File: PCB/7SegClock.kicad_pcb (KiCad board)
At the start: 2 copper layers, 19 parts, among them CON1 USB-MINI-B, Q1 NPN, U1 P8X32A, U2 24LC256, U3 FT232RL, U4 DS3231, U6 DS3231, X1 5mhz CRYSTAL

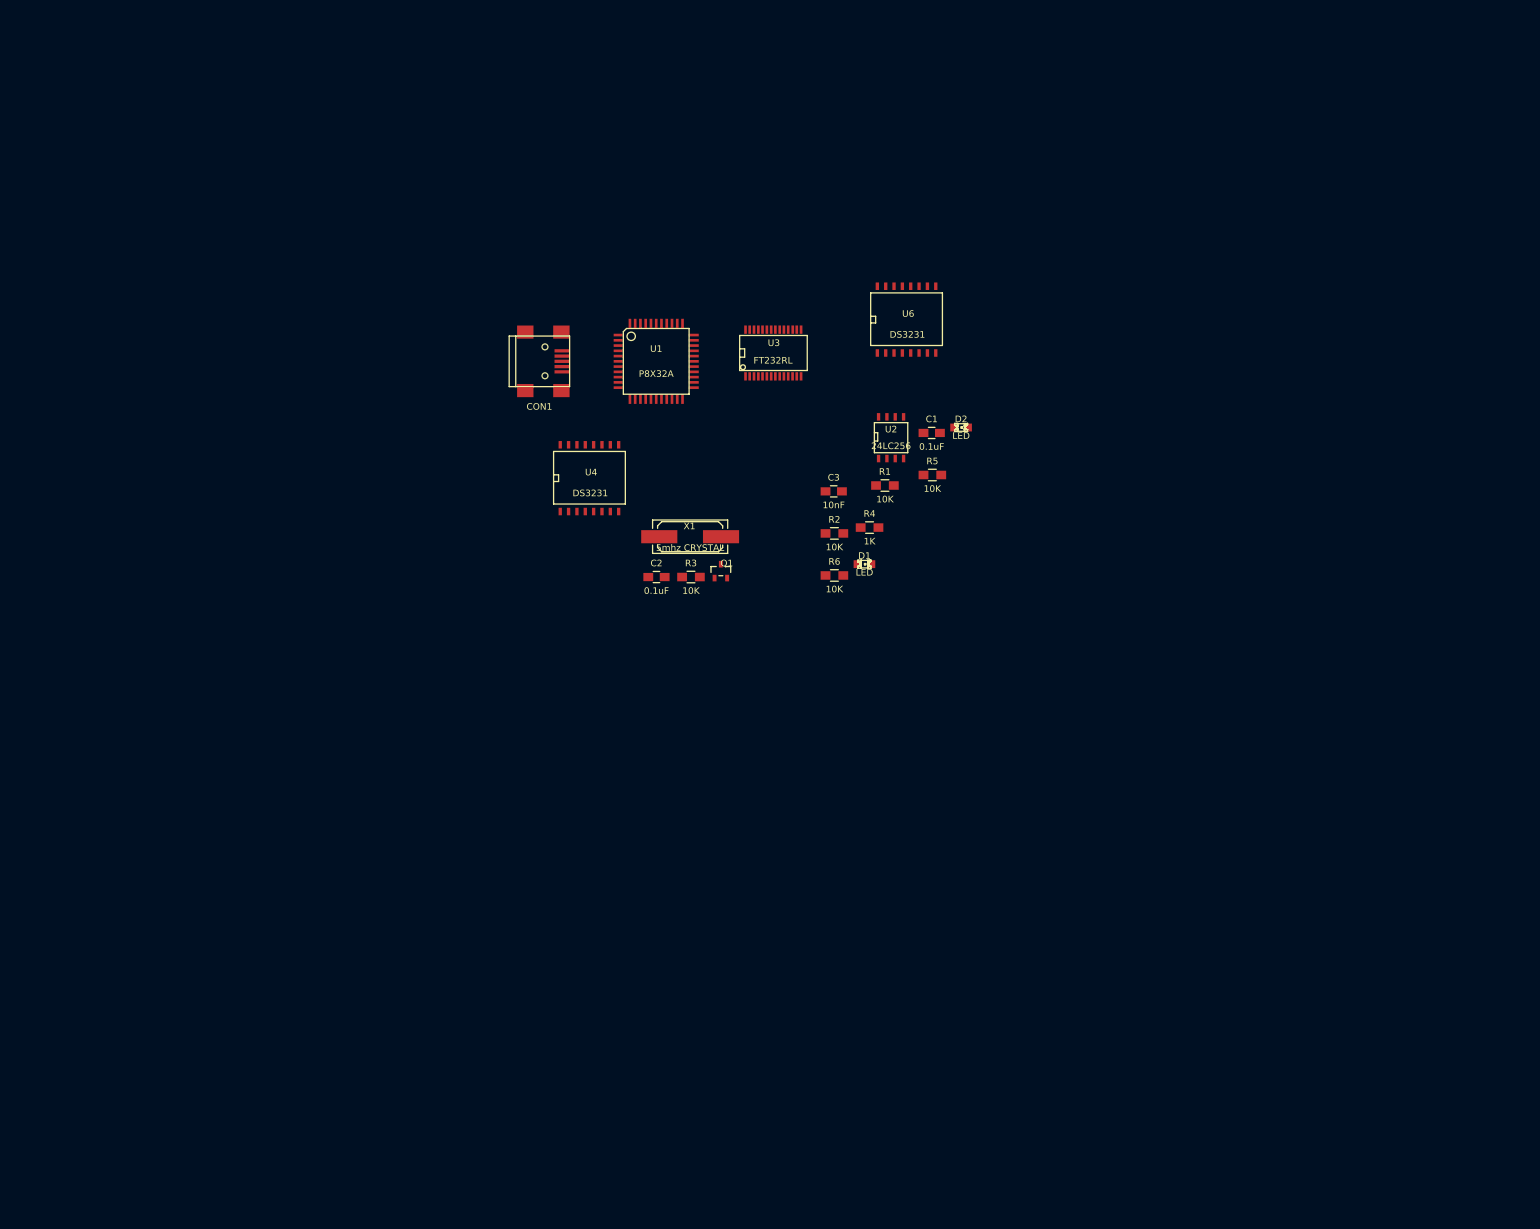
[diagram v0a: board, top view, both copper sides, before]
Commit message: Worked on PCB, added FPGA.
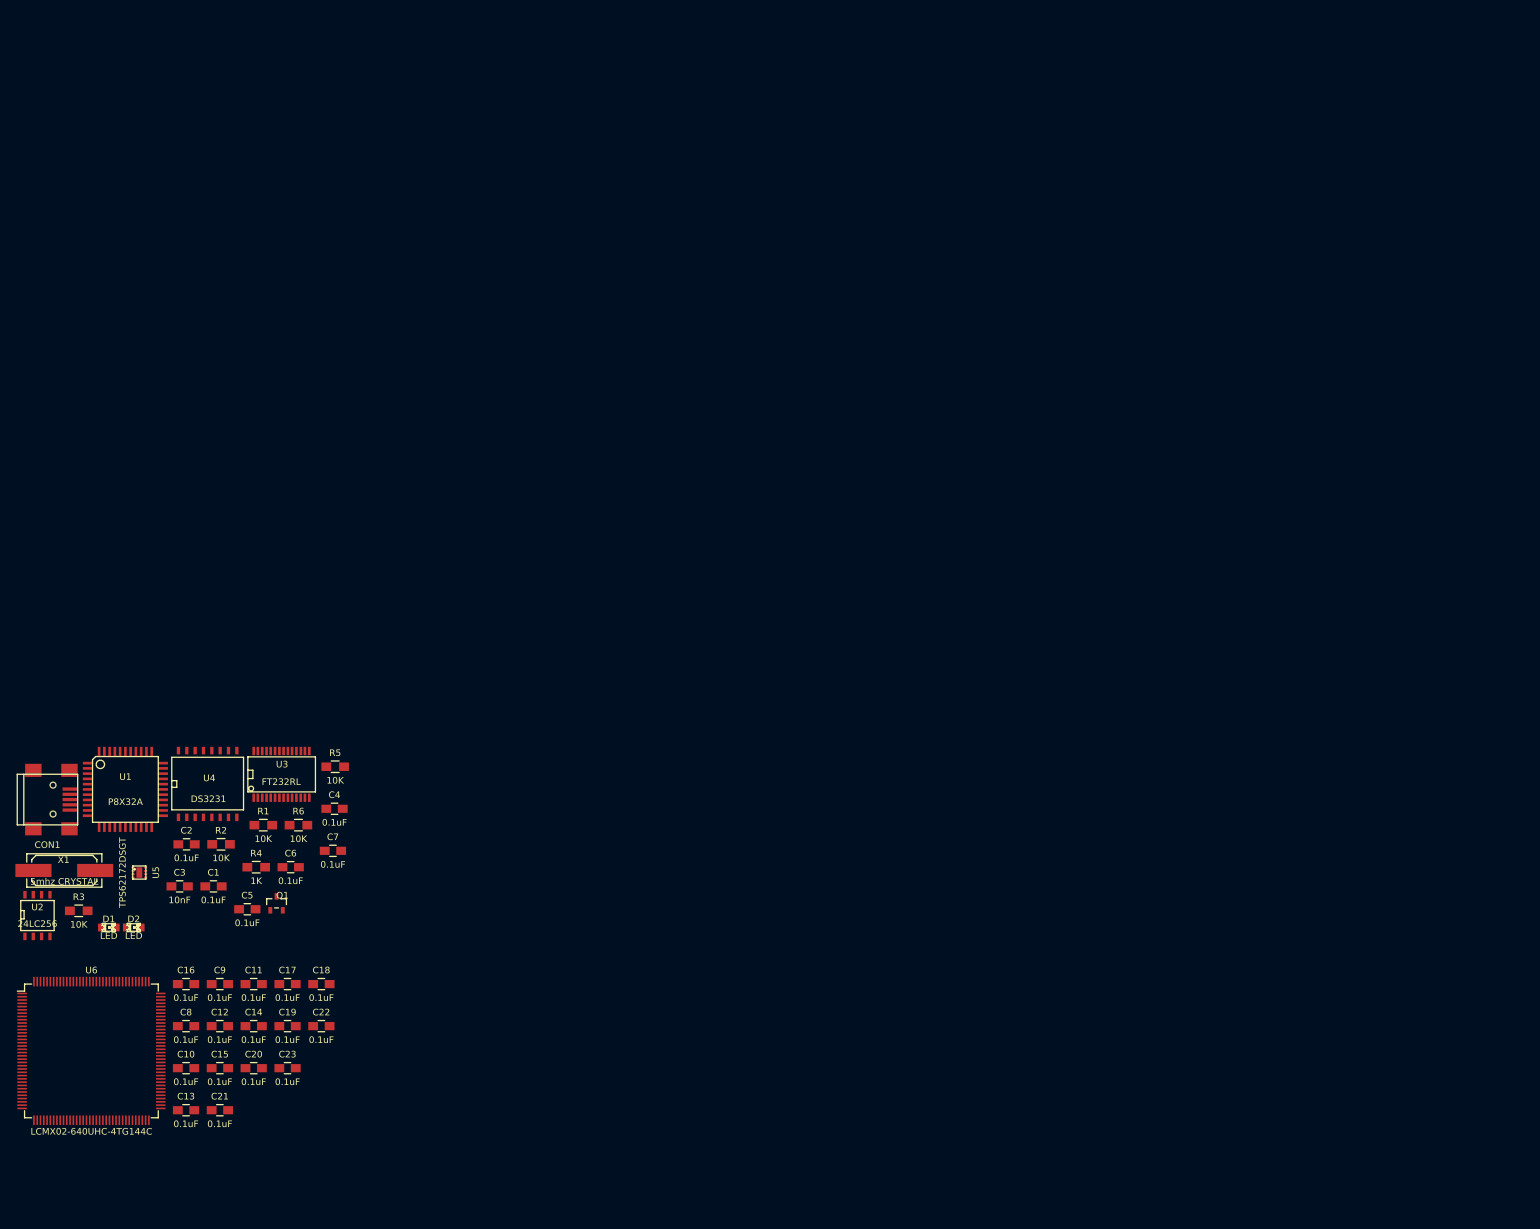
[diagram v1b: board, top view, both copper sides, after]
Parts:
- added C10: 0.1uF, Capacitors_SMD:C_0805_HandSoldering, F.Cu at (49.1, 178.7)
- added C11: 0.1uF, Capacitors_SMD:C_0805_HandSoldering, F.Cu at (59.4, 165.9)
- added C12: 0.1uF, Capacitors_SMD:C_0805_HandSoldering, F.Cu at (54.2, 172.3)
- added C13: 0.1uF, Capacitors_SMD:C_0805_HandSoldering, F.Cu at (49.1, 185.1)
- added C14: 0.1uF, Capacitors_SMD:C_0805_HandSoldering, F.Cu at (59.4, 172.3)
- added C15: 0.1uF, Capacitors_SMD:C_0805_HandSoldering, F.Cu at (54.2, 178.7)
- added C16: 0.1uF, Capacitors_SMD:C_0805_HandSoldering, F.Cu at (49.1, 165.9)
- added C17: 0.1uF, Capacitors_SMD:C_0805_HandSoldering, F.Cu at (64.5, 165.9)
- added C18: 0.1uF, Capacitors_SMD:C_0805_HandSoldering, F.Cu at (69.7, 165.9)
- added C19: 0.1uF, Capacitors_SMD:C_0805_HandSoldering, F.Cu at (64.5, 172.3)
- added C20: 0.1uF, Capacitors_SMD:C_0805_HandSoldering, F.Cu at (59.4, 178.7)
- added C21: 0.1uF, Capacitors_SMD:C_0805_HandSoldering, F.Cu at (54.2, 185.1)
- added C22: 0.1uF, Capacitors_SMD:C_0805_HandSoldering, F.Cu at (69.7, 172.3)
- added C23: 0.1uF, Capacitors_SMD:C_0805_HandSoldering, F.Cu at (64.5, 178.7)
- added C4: 0.1uF, Capacitors_SMD:C_0805_HandSoldering, F.Cu at (71.7, 139.2)
- added C5: 0.1uF, Capacitors_SMD:C_0805_HandSoldering, F.Cu at (58.4, 154.5)
- added C6: 0.1uF, Capacitors_SMD:C_0805_HandSoldering, F.Cu at (65.0, 148.1)
- added C7: 0.1uF, Capacitors_SMD:C_0805_HandSoldering, F.Cu at (71.4, 145.6)
- added C8: 0.1uF, Capacitors_SMD:C_0805_HandSoldering, F.Cu at (49.1, 172.3)
- added C9: 0.1uF, Capacitors_SMD:C_0805_HandSoldering, F.Cu at (54.2, 165.9)
- added U5: TPS62172DSGT, SMD_Packages:WSON-8-1EP, F.Cu at (42.0, 148.9)
- U6: value DS3231 -> LCMX02-640UHC-4TG144C; footprint SMD_Packages:SO-16-W -> Housings_QFP:TQFP-144_20x20mm_Pitch0.5mm
- moved U6 166.7 mm to (34.7, 176.1)
- moved U2 148.9 mm to (26.5, 155.5)
- moved D2 147.1 mm to (41.1, 157.3)
- moved C1 129.3 mm to (53.3, 151.0)
- moved D1 127.6 mm to (37.3, 157.3)
- moved C3 116.3 mm to (48.1, 151.0)
- moved X1 108.0 mm to (30.6, 148.6)
- moved R1 107.8 mm to (60.8, 141.7)
- moved R4 106.7 mm to (59.8, 148.1)
- moved R3 106.1 mm to (32.8, 154.7)
- moved R2 104.7 mm to (54.4, 144.6)
- moved U1 103.8 mm to (39.9, 136.3)
- moved R5 101.2 mm to (71.8, 132.8)
- moved CON1 100.3 mm to (28.0, 137.8)
- moved U3 98.6 mm to (63.6, 134.0)
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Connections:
- net /Lattice MACHXO2/RST renamed Net-(U6-Pad4)
- net Net-(U1-Pad20) renamed /Lattice MACHXO2/CS_PWM
- net Net-(U1-Pad21) renamed /Lattice MACHXO2/CS_Clock
- net Net-(U1-Pad22) renamed /Lattice MACHXO2/CLK
- net Net-(U1-Pad23) renamed /Lattice MACHXO2/DataOUT
- net Net-(U1-Pad24) renamed /Lattice MACHXO2/DataIN
- U1 pad 19: /Lattice MACHXO2/P16 -> /Lattice MACHXO2/CS_Encoder
- U6 pad 16: /Lattice MACHXO2/P16 -> +3V3
- U6 pad 7: Net-(U6-Pad7) -> +3V3
- U6 pad 8: Net-(U6-Pad8) -> GND

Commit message: Worked on PCB.
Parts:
- C1, C10, C11, C12, C13, C14, C15, C16, C17, C18, C19, C2, C20, C21, C22, C23, C3, C4, C5, C6, C7, C8, C9: footprint Capacitors_SMD:C_0805_HandSoldering -> Capacitors_SMD:C_0603_HandSoldering
- R1, R2, R3, R4, R5, R6: footprint Resistors_SMD:R_0805_HandSoldering -> Resistors_SMD:R_0603_HandSoldering
- U1, U6: moved to B.Cu
- moved C10 166.3 mm to (188.8, 88.5)
- moved C16 166.3 mm to (188.8, 75.7)
- moved C8 166.3 mm to (188.8, 82.1)
- moved C11 166.3 mm to (199.1, 75.7)
- moved C12 166.3 mm to (193.9, 82.1)
- moved C13 166.3 mm to (188.8, 94.9)
- moved C14 166.3 mm to (199.1, 82.1)
- moved C15 166.3 mm to (193.9, 88.5)
- moved C17 166.3 mm to (204.2, 75.7)
- moved C18 166.3 mm to (209.4, 75.7)
- moved C19 166.3 mm to (204.2, 82.1)
- moved C20 166.3 mm to (199.1, 88.5)
- moved C21 166.3 mm to (193.9, 94.9)
- moved C22 166.3 mm to (209.4, 82.1)
- moved C23 166.3 mm to (204.2, 88.5)
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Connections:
- U6 pad 100: (no net) -> Net-(U6-Pad100)
- U6 pad 101: (no net) -> GND
- U6 pad 102: (no net) -> +3V3
- U6 pad 103: (no net) -> Net-(U6-Pad103)
- U6 pad 104: (no net) -> Net-(U6-Pad104)
- U6 pad 105: (no net) -> Net-(U6-Pad105)
- U6 pad 106: (no net) -> Net-(U6-Pad106)
- U6 pad 107: (no net) -> Net-(U6-Pad107)
- U6 pad 108: (no net) -> +3V3
- U6 pad 109: (no net) -> /Lattice MACHXO2/DataIN
- U6 pad 110: (no net) -> /Lattice MACHXO2/DataOUT
- U6 pad 111: (no net) -> /Lattice MACHXO2/CLK
- U6 pad 112: (no net) -> /Lattice MACHXO2/CS_Clock
- U6 pad 113: (no net) -> /Lattice MACHXO2/CS_PWM
- U6 pad 114: (no net) -> /Lattice MACHXO2/CS_Encoder
- U6 pad 115: (no net) -> Net-(U6-Pad115)
- U6 pad 116: (no net) -> GND
- U6 pad 117: (no net) -> Net-(U6-Pad117)
- U6 pad 118: (no net) -> +3V3
- U6 pad 119: (no net) -> Net-(U6-Pad119)
- U6 pad 120: (no net) -> Net-(U6-Pad120)
- U6 pad 121: (no net) -> Net-(U6-Pad121)
- U6 pad 122: (no net) -> Net-(U6-Pad122)
- U6 pad 123: (no net) -> +3V3
- U6 pad 124: (no net) -> GND
- U6 pad 125: (no net) -> SDA
- U6 pad 126: (no net) -> SCL
- U6 pad 127: (no net) -> Net-(U6-Pad127)
- U6 pad 128: (no net) -> Net-(U6-Pad128)
- U6 pad 129: (no net) -> Net-(U6-Pad129)
- U6 pad 130: (no net) -> /Lattice MACHXO2/TMS
- U6 pad 131: (no net) -> /Lattice MACHXO2/TCK
- U6 pad 132: (no net) -> Net-(U6-Pad132)
- U6 pad 133: (no net) -> Net-(U6-Pad133)
- U6 pad 134: (no net) -> GND
- U6 pad 135: (no net) -> +3V3
- U6 pad 136: (no net) -> /Lattice MACHXO2/TDI
- U6 pad 137: (no net) -> /Lattice MACHXO2/TDO
- U6 pad 138: (no net) -> Net-(U6-Pad138)
- U6 pad 139: (no net) -> Net-(U6-Pad139)
- U6 pad 140: (no net) -> Net-(U6-Pad140)
- U6 pad 141: (no net) -> Net-(U6-Pad141)
- U6 pad 142: (no net) -> Net-(U6-Pad142)
- U6 pad 143: (no net) -> Net-(U6-Pad143)
- U6 pad 144: (no net) -> +3V3
- U6 pad 17: (no net) -> Net-(U6-Pad17)
- U6 pad 18: (no net) -> GND
- U6 pad 19: (no net) -> Net-(U6-Pad19)
- U6 pad 20: (no net) -> Net-(U6-Pad20)
- U6 pad 21: (no net) -> Net-(U6-Pad21)
- U6 pad 22: (no net) -> Net-(U6-Pad22)
- U6 pad 23: (no net) -> Net-(U6-Pad23)
- U6 pad 24: (no net) -> Net-(U6-Pad24)
- U6 pad 25: (no net) -> Net-(U6-Pad25)
- U6 pad 26: (no net) -> Net-(U6-Pad26)
- U6 pad 27: (no net) -> Net-(U6-Pad27)
- U6 pad 28: (no net) -> Net-(U6-Pad28)
- U6 pad 29: (no net) -> GND
- U6 pad 30: (no net) -> +3V3
- U6 pad 31: (no net) -> Net-(U6-Pad31)
- U6 pad 32: (no net) -> Net-(U6-Pad32)
- U6 pad 33: (no net) -> Net-(U6-Pad33)
- U6 pad 34: (no net) -> Net-(U6-Pad34)
- U6 pad 35: (no net) -> Net-(U6-Pad35)
- U6 pad 36: (no net) -> +3V3
- U6 pad 37: (no net) -> +3V3
- U6 pad 38: (no net) -> Net-(U6-Pad38)
- U6 pad 39: (no net) -> Net-(U6-Pad39)
- U6 pad 40: (no net) -> Net-(U6-Pad40)
- U6 pad 41: (no net) -> Net-(U6-Pad41)
- U6 pad 42: (no net) -> Net-(U6-Pad42)
- U6 pad 43: (no net) -> Net-(U6-Pad43)
- U6 pad 44: (no net) -> Net-(U6-Pad44)
- U6 pad 45: (no net) -> Net-(U6-Pad45)
- U6 pad 46: (no net) -> GND
- U6 pad 47: (no net) -> Net-(U6-Pad47)
- U6 pad 48: (no net) -> Net-(U6-Pad48)
- U6 pad 49: (no net) -> Net-(U6-Pad49)
- U6 pad 50: (no net) -> Net-(U6-Pad50)
- U6 pad 51: (no net) -> +3V3
- U6 pad 52: (no net) -> Net-(U6-Pad52)
- U6 pad 53: (no net) -> GND
- U6 pad 54: (no net) -> Net-(U6-Pad54)
- U6 pad 55: (no net) -> Net-(U6-Pad55)
- U6 pad 56: (no net) -> Net-(U6-Pad56)
- U6 pad 57: (no net) -> Net-(U6-Pad57)
- U6 pad 58: (no net) -> Net-(U6-Pad58)
- U6 pad 59: (no net) -> Net-(U6-Pad59)
- U6 pad 60: (no net) -> Net-(U6-Pad60)
- U6 pad 61: (no net) -> Net-(U6-Pad61)
- U6 pad 62: (no net) -> Net-(U6-Pad62)
- U6 pad 63: (no net) -> Net-(U6-Pad63)
- U6 pad 64: (no net) -> GND
- U6 pad 65: (no net) -> Net-(U6-Pad65)
- U6 pad 66: (no net) -> +3V3
- U6 pad 67: (no net) -> Net-(U6-Pad67)
- U6 pad 68: (no net) -> Net-(U6-Pad68)
- U6 pad 69: (no net) -> Net-(U6-Pad69)
- U6 pad 70: (no net) -> Net-(U6-Pad70)
- U6 pad 71: (no net) -> Net-(U6-Pad71)
- U6 pad 72: (no net) -> +3V3
- U6 pad 73: (no net) -> Net-(U6-Pad73)
- U6 pad 74: (no net) -> Net-(U6-Pad74)
- U6 pad 75: (no net) -> Net-(U6-Pad75)
- U6 pad 76: (no net) -> Net-(U6-Pad76)
- U6 pad 77: (no net) -> Net-(U6-Pad77)
- U6 pad 78: (no net) -> Net-(U6-Pad78)
- U6 pad 79: (no net) -> +3V3
- U6 pad 80: (no net) -> GND
- U6 pad 81: (no net) -> Net-(U6-Pad81)
- U6 pad 82: (no net) -> Net-(U6-Pad82)
- U6 pad 83: (no net) -> Net-(U6-Pad83)
- U6 pad 84: (no net) -> Net-(U6-Pad84)
- U6 pad 85: (no net) -> Net-(U6-Pad85)
- U6 pad 86: (no net) -> Net-(U6-Pad86)
- U6 pad 87: (no net) -> Net-(U6-Pad87)
- U6 pad 88: (no net) -> +3V3
- U6 pad 89: (no net) -> Net-(U6-Pad89)
- U6 pad 90: (no net) -> GND
- U6 pad 91: (no net) -> Net-(U6-Pad91)
- U6 pad 92: (no net) -> Net-(U6-Pad92)
- U6 pad 93: (no net) -> Net-(U6-Pad93)
- U6 pad 94: (no net) -> Net-(U6-Pad94)
- U6 pad 95: (no net) -> Net-(U6-Pad95)
- U6 pad 96: (no net) -> Net-(U6-Pad96)
- U6 pad 97: (no net) -> Net-(U6-Pad97)
- U6 pad 98: (no net) -> Net-(U6-Pad98)
- U6 pad 99: (no net) -> Net-(U6-Pad99)
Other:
- board outline added: 177.8 x 76.2 mm
